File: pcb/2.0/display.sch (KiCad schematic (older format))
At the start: 3 parts

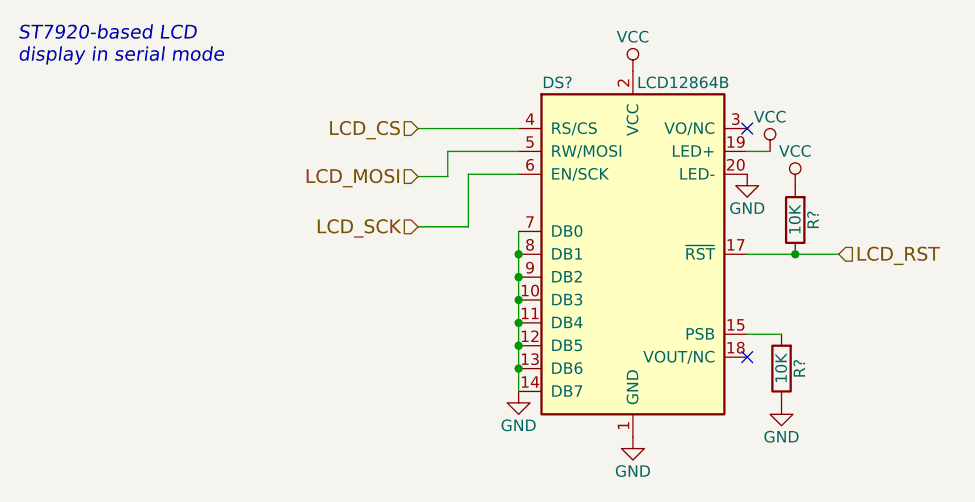
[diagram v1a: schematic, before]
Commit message: add the sound circuit
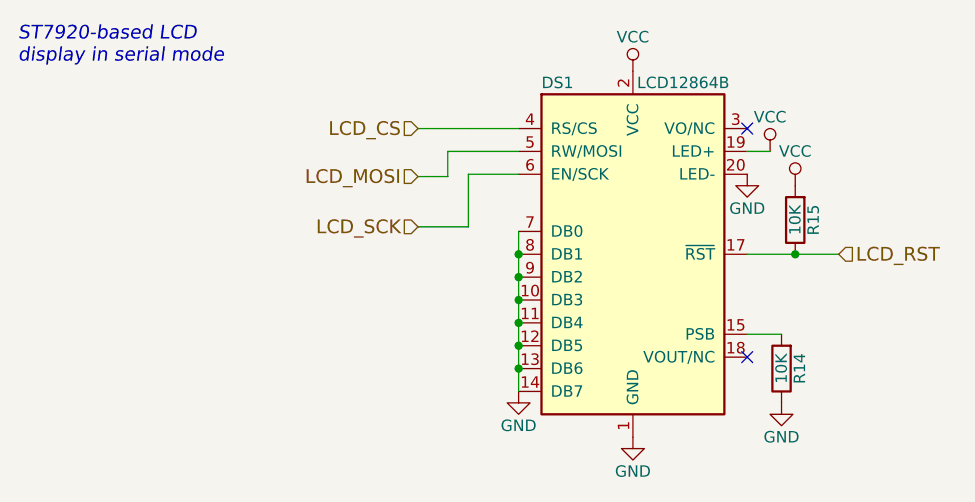
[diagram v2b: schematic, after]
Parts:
- gave numbers to parts that had none: 3
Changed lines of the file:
@@
 $EndDescr
 $Comp
-L LCD12864B DS?
+L LCD12864B DS1
 U 1 1 5A311520
 P 6070 3340
-F 0 "DS?" H 5740 4090 50  0000 C CNN
+F 0 "DS1" H 5740 4090 50  0000 C CNN
 F 1 "LCD12864B" H 6290 4090 50  0000 C CNN
 F 2 "kamaji:LCD12864B" H 6070 2440 50  0001 C CIN
@@
 $EndComp
 $Comp
-L GND #PWR?
+L GND #PWR44
 U 1 1 5A311527
 P 6070 4140
-F 0 "#PWR?" H 6070 3890 50  0001 C CNN
+F 0 "#PWR44" H 6070 3890 50  0001 C CNN
 F 1 "GND" H 6070 3990 50  0000 C CNN
 F 2 "" H 6070 4140 50  0001 C CNN
@@
 $EndComp
 $Comp
-L VCC #PWR?
+L VCC #PWR43
 U 1 1 5A31152D
 P 6070 2540
-F 0 "#PWR?" H 6070 2390 50  0001 C CNN
+F 0 "#PWR43" H 6070 2390 50  0001 C CNN
 F 1 "VCC" H 6070 2690 50  0000 C CNN
 F 2 "" H 6070 2540 50  0001 C CNN
@@
 NoConn ~ 6570 2790
 $Comp
-L VCC #PWR?
+L VCC #PWR46
 U 1 1 5A311544
 P 6670 2890
-F 0 "#PWR?" H 6670 2740 50  0001 C CNN
+F 0 "#PWR46" H 6670 2740 50  0001 C CNN
 F 1 "VCC" H 6670 3040 50  0000 C CNN
 F 2 "" H 6670 2890 50  0001 C CNN
@@
 	6570 2890 6670 2890
 $Comp
-L GND #PWR?
+L GND #PWR45
 U 1 1 5A31154B
 P 6570 2990
-F 0 "#PWR?" H 6570 2740 50  0001 C CNN
+F 0 "#PWR45" H 6570 2740 50  0001 C CNN
 F 1 "GND" H 6570 2840 50  0000 C CNN
 F 2 "" H 6570 2990 50  0001 C CNN
@@
 $EndComp
 $Comp
-L VCC #PWR?
+L VCC #PWR48
 U 1 1 5A311551
 P 6780 3040
-F 0 "#PWR?" H 6780 2890 50  0001 C CNN
+F 0 "#PWR48" H 6780 2890 50  0001 C CNN
 F 1 "VCC" H 6780 3190 50  0000 C CNN
 F 2 "" H 6780 3040 50  0001 C CNN
@@
 $EndComp
 $Comp
-L R R?
+L R R15
 U 1 1 5A311557
 P 6780 3190
-F 0 "R?" V 6700 3190 50  0000 C CNN
+F 0 "R15" V 6700 3190 50  0000 C CNN
 F 1 "10K" V 6780 3190 50  0000 C CNN
 F 2 "" V 6710 3190 50  0001 C CNN
@@
 NoConn ~ 6570 3790
 $Comp
-L R R?
+L R R14
 U 1 1 5A311573
 P 6720 3840
-F 0 "R?" V 6640 3840 50  0000 C CNN
+F 0 "R14" V 6640 3840 50  0000 C CNN
 F 1 "10K" V 6720 3840 50  0000 C CNN
 F 2 "" V 6650 3840 50  0001 C CNN
@@
 $EndComp
 $Comp
-L GND #PWR?
+L GND #PWR47
 U 1 1 5A31157A
 P 6720 3990
-F 0 "#PWR?" H 6720 3740 50  0001 C CNN
+F 0 "#PWR47" H 6720 3740 50  0001 C CNN
 F 1 "GND" H 6720 3840 50  0000 C CNN
 F 2 "" H 6720 3990 50  0001 C CNN
@@
 ST7920-based LCD\ndisplay in serial mode
 $Comp
-L GND #PWR?
+L GND #PWR42
 U 1 1 5A311585
 P 5570 3940
-F 0 "#PWR?" H 5570 3690 50  0001 C CNN
+F 0 "#PWR42" H 5570 3690 50  0001 C CNN
 F 1 "GND" H 5570 3790 50  0000 C CNN
 F 2 "" H 5570 3940 50  0001 C CNN

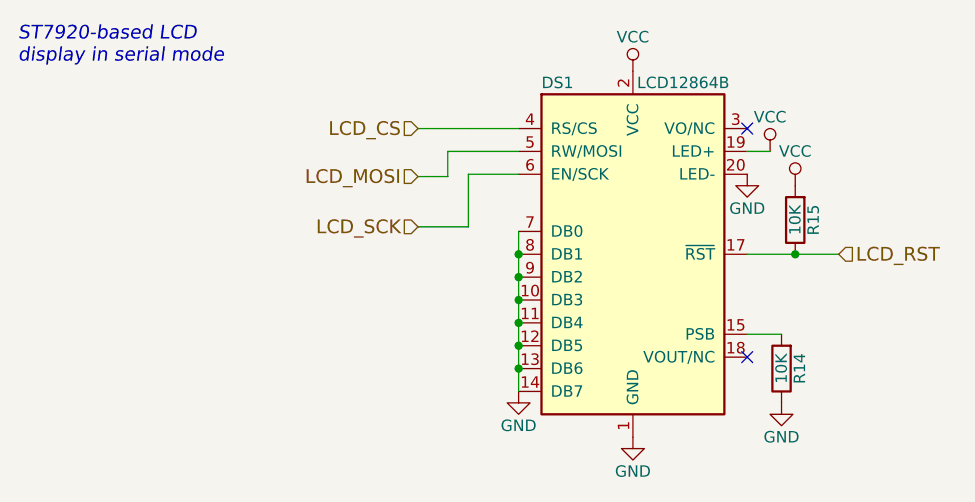
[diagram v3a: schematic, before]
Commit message: complete the 2.0 schematic
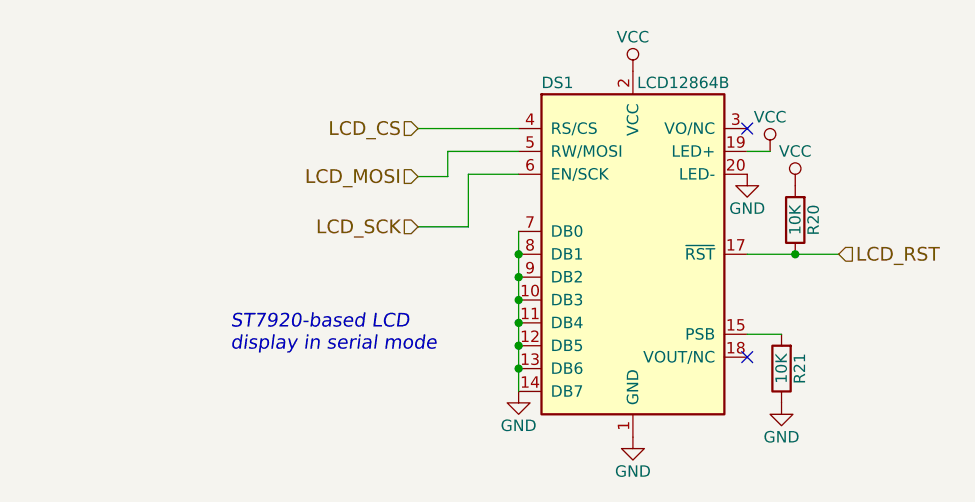
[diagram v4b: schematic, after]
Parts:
- renumbered R15 to R20, R14 to R21
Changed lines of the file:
@@
 $EndComp
 $Comp
-L GND #PWR44
+L GND #PWR042
 U 1 1 5A311527
 P 6070 4140
-F 0 "#PWR44" H 6070 3890 50  0001 C CNN
+F 0 "#PWR042" H 6070 3890 50  0001 C CNN
 F 1 "GND" H 6070 3990 50  0000 C CNN
 F 2 "" H 6070 4140 50  0001 C CNN
@@
 $EndComp
 $Comp
-L VCC #PWR43
+L VCC #PWR043
 U 1 1 5A31152D
 P 6070 2540
-F 0 "#PWR43" H 6070 2390 50  0001 C CNN
+F 0 "#PWR043" H 6070 2390 50  0001 C CNN
 F 1 "VCC" H 6070 2690 50  0000 C CNN
 F 2 "" H 6070 2540 50  0001 C CNN
@@
 $EndComp
 Wire Wire Line
-	5570 3240 5570 3340
-Wire Wire Line
-	5570 3340 5570 3440
-Wire Wire Line
-	5570 3440 5570 3540
-Wire Wire Line
-	5570 3540 5570 3640
-Wire Wire Line
-	5570 3640 5570 3740
-Wire Wire Line
-	5570 3740 5570 3840
-Wire Wire Line
-	5570 3840 5570 3940
+	5570 3240 5570 3940
 Connection ~ 5570 3340
 Connection ~ 5570 3440
@@
 NoConn ~ 6570 2790
 $Comp
-L VCC #PWR46
+L VCC #PWR044
 U 1 1 5A311544
 P 6670 2890
-F 0 "#PWR46" H 6670 2740 50  0001 C CNN
+F 0 "#PWR044" H 6670 2740 50  0001 C CNN
 F 1 "VCC" H 6670 3040 50  0000 C CNN
 F 2 "" H 6670 2890 50  0001 C CNN
@@
 	6570 2890 6670 2890
 $Comp
-L GND #PWR45
+L GND #PWR045
 U 1 1 5A31154B
 P 6570 2990
-F 0 "#PWR45" H 6570 2740 50  0001 C CNN
+F 0 "#PWR045" H 6570 2740 50  0001 C CNN
 F 1 "GND" H 6570 2840 50  0000 C CNN
 F 2 "" H 6570 2990 50  0001 C CNN
@@
 $EndComp
 $Comp
-L VCC #PWR48
+L VCC #PWR046
 U 1 1 5A311551
 P 6780 3040
-F 0 "#PWR48" H 6780 2890 50  0001 C CNN
+F 0 "#PWR046" H 6780 2890 50  0001 C CNN
 F 1 "VCC" H 6780 3190 50  0000 C CNN
 F 2 "" H 6780 3040 50  0001 C CNN
@@
 $EndComp
 $Comp
-L R R15
+L R R20
 U 1 1 5A311557
 P 6780 3190
-F 0 "R15" V 6700 3190 50  0000 C CNN
+F 0 "R20" V 6700 3190 50  0000 C CNN
 F 1 "10K" V 6780 3190 50  0000 C CNN
 F 2 "" V 6710 3190 50  0001 C CNN
@@
 NoConn ~ 6570 3790
 $Comp
-L R R14
+L R R21
 U 1 1 5A311573
 P 6720 3840
-F 0 "R14" V 6640 3840 50  0000 C CNN
+F 0 "R21" V 6640 3840 50  0000 C CNN
 F 1 "10K" V 6720 3840 50  0000 C CNN
 F 2 "" V 6650 3840 50  0001 C CNN
@@
 $EndComp
 $Comp
-L GND #PWR47
+L GND #PWR047
 U 1 1 5A31157A
 P 6720 3990
-F 0 "#PWR47" H 6720 3740 50  0001 C CNN
+F 0 "#PWR047" H 6720 3740 50  0001 C CNN
 F 1 "GND" H 6720 3840 50  0000 C CNN
 F 2 "" H 6720 3990 50  0001 C CNN
@@
 $EndComp
 Wire Wire Line
-	6570 3340 6780 3340
-Wire Wire Line
-	6780 3340 6970 3340
+	6570 3340 6970 3340
 Connection ~ 6780 3340
 Wire Wire Line
 	6570 3690 6720 3690
-Text Notes 3380 2510 0    60   Italic 0
+Text Notes 4310 3770 0    60   Italic 0
 ST7920-based LCD\ndisplay in serial mode
 $Comp
-L GND #PWR42
+L GND #PWR048
 U 1 1 5A311585
 P 5570 3940
-F 0 "#PWR42" H 5570 3690 50  0001 C CNN
+F 0 "#PWR048" H 5570 3690 50  0001 C CNN
 F 1 "GND" H 5570 3790 50  0000 C CNN
 F 2 "" H 5570 3940 50  0001 C CNN
@@
 	5350 3220 5350 2990
 Wire Wire Line
-	5130 2790 5360 2790
-Wire Wire Line
-	5360 2790 5570 2790
+	5130 2790 5570 2790
 $EndSCHEMATC
